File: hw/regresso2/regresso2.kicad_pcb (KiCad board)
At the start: 2 copper layers, 48.9 x 53.3 mm, 35 parts, among them CN5 Conn_01x10, CN6 Conn_01x08, CN8 Conn_01x06, CN9 Conn_01x08, J1 CONN_01X02, P10 CONTROL, P9 FX2LA, U1 STM32F303CCTx, U2 MIC550x-3.3YM5, Y1 Crystal_GND24_Small

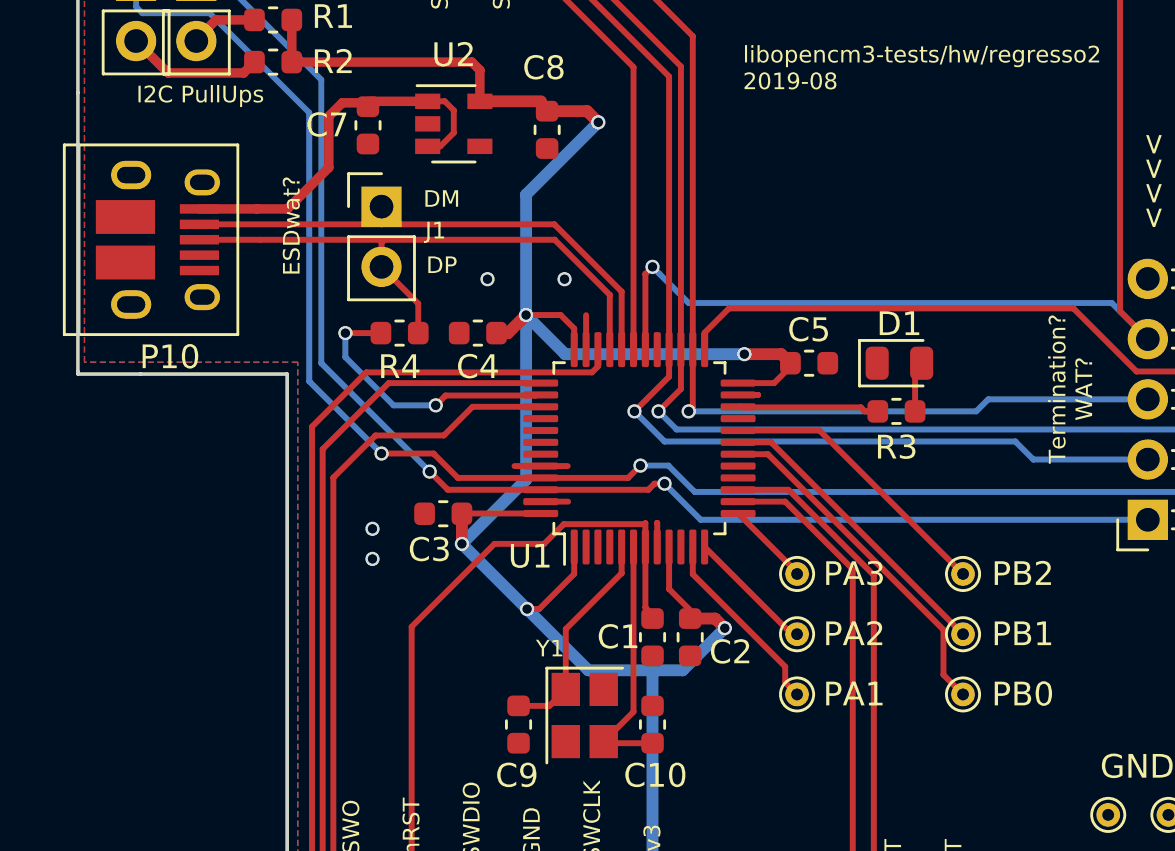
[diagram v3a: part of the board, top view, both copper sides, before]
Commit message: regresso2: update parts for seeed assembly.
Still a little more expensive than I'd hoped.  and I don't have the
parts to do it myself.  but hey, try it out? toy money?
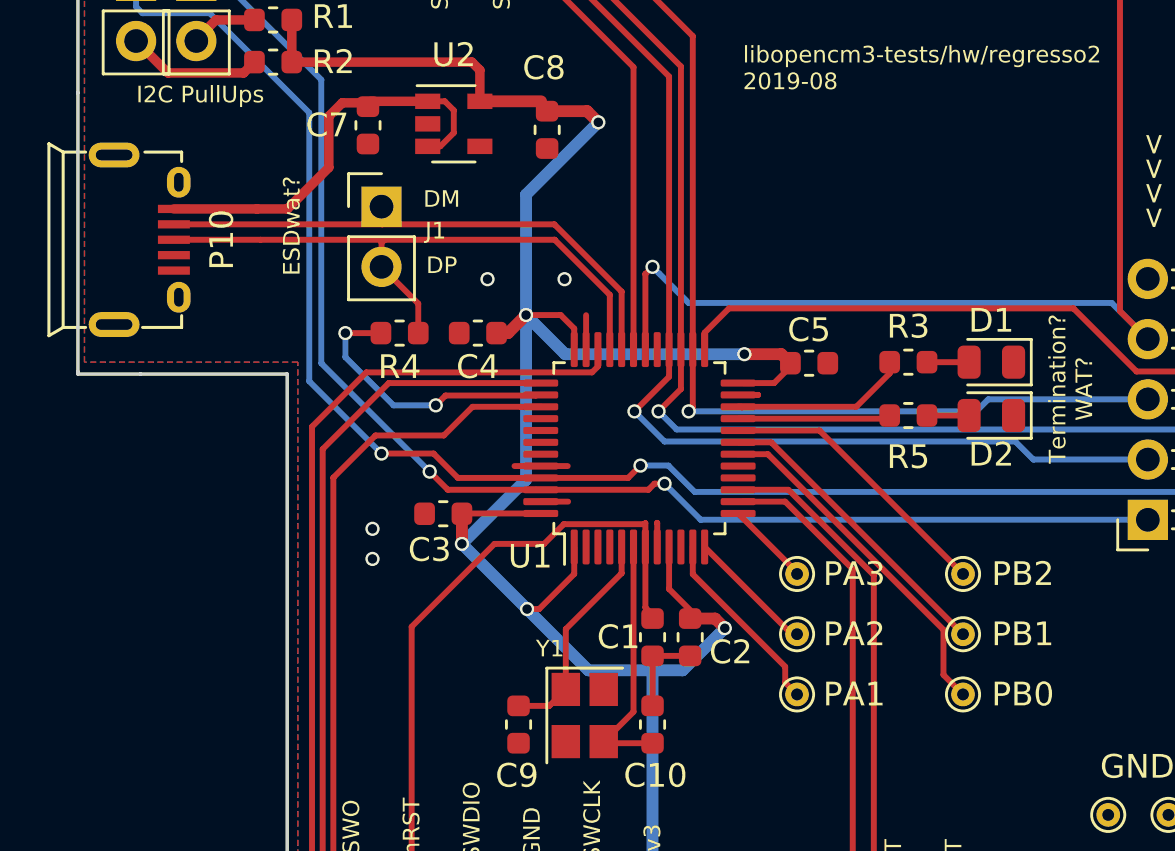
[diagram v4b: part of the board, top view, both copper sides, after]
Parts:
- added D2: red, LED_SMD:LED_0805_2012Metric, F.Cu at (166.6, 99.6)
- added R5: 1.5k, Resistor_SMD:R_0603_1608Metric, F.Cu at (163.1, 99.6)
- D1: value indicator -> green
- P10: footprint Connectors:USB_Micro-B_10103594-0001LF -> OPL_Connector:MICRO-USB5+6P-SMD-0.65-AB
- R3: value 1k -> 1.5k
- moved D1 3.88 mm to (166.6, 97.4), turned to 180 degrees
- moved R3 2.14 mm to (163.1, 97.4)
- moved P10 2.10 mm to (129.6, 92.2)
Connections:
- net /LED renamed /LED_G
- P10 pad 6: Net-(P10-Pad6) -> (no net)
- U1 pad 21: (no net) -> /LED_R
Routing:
- net /LED_R: track 0.00 -> 6.45 mm
- net GND: track 6.72 -> 10.4 mm
- net Net-(D2-Pad2): track 0.00 -> 1.78 mm
- net /LED_G: track 5.97 -> 7.62 mm
- net /USB_DM: track 22.0 -> 23.1 mm
- net /USB_DP: track 25.0 -> 26.1 mm
- net +5V: track 16.5 -> 17.6 mm
